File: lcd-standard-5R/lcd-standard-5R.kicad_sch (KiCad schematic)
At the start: 12 parts, among them U1 siplex-som-s16

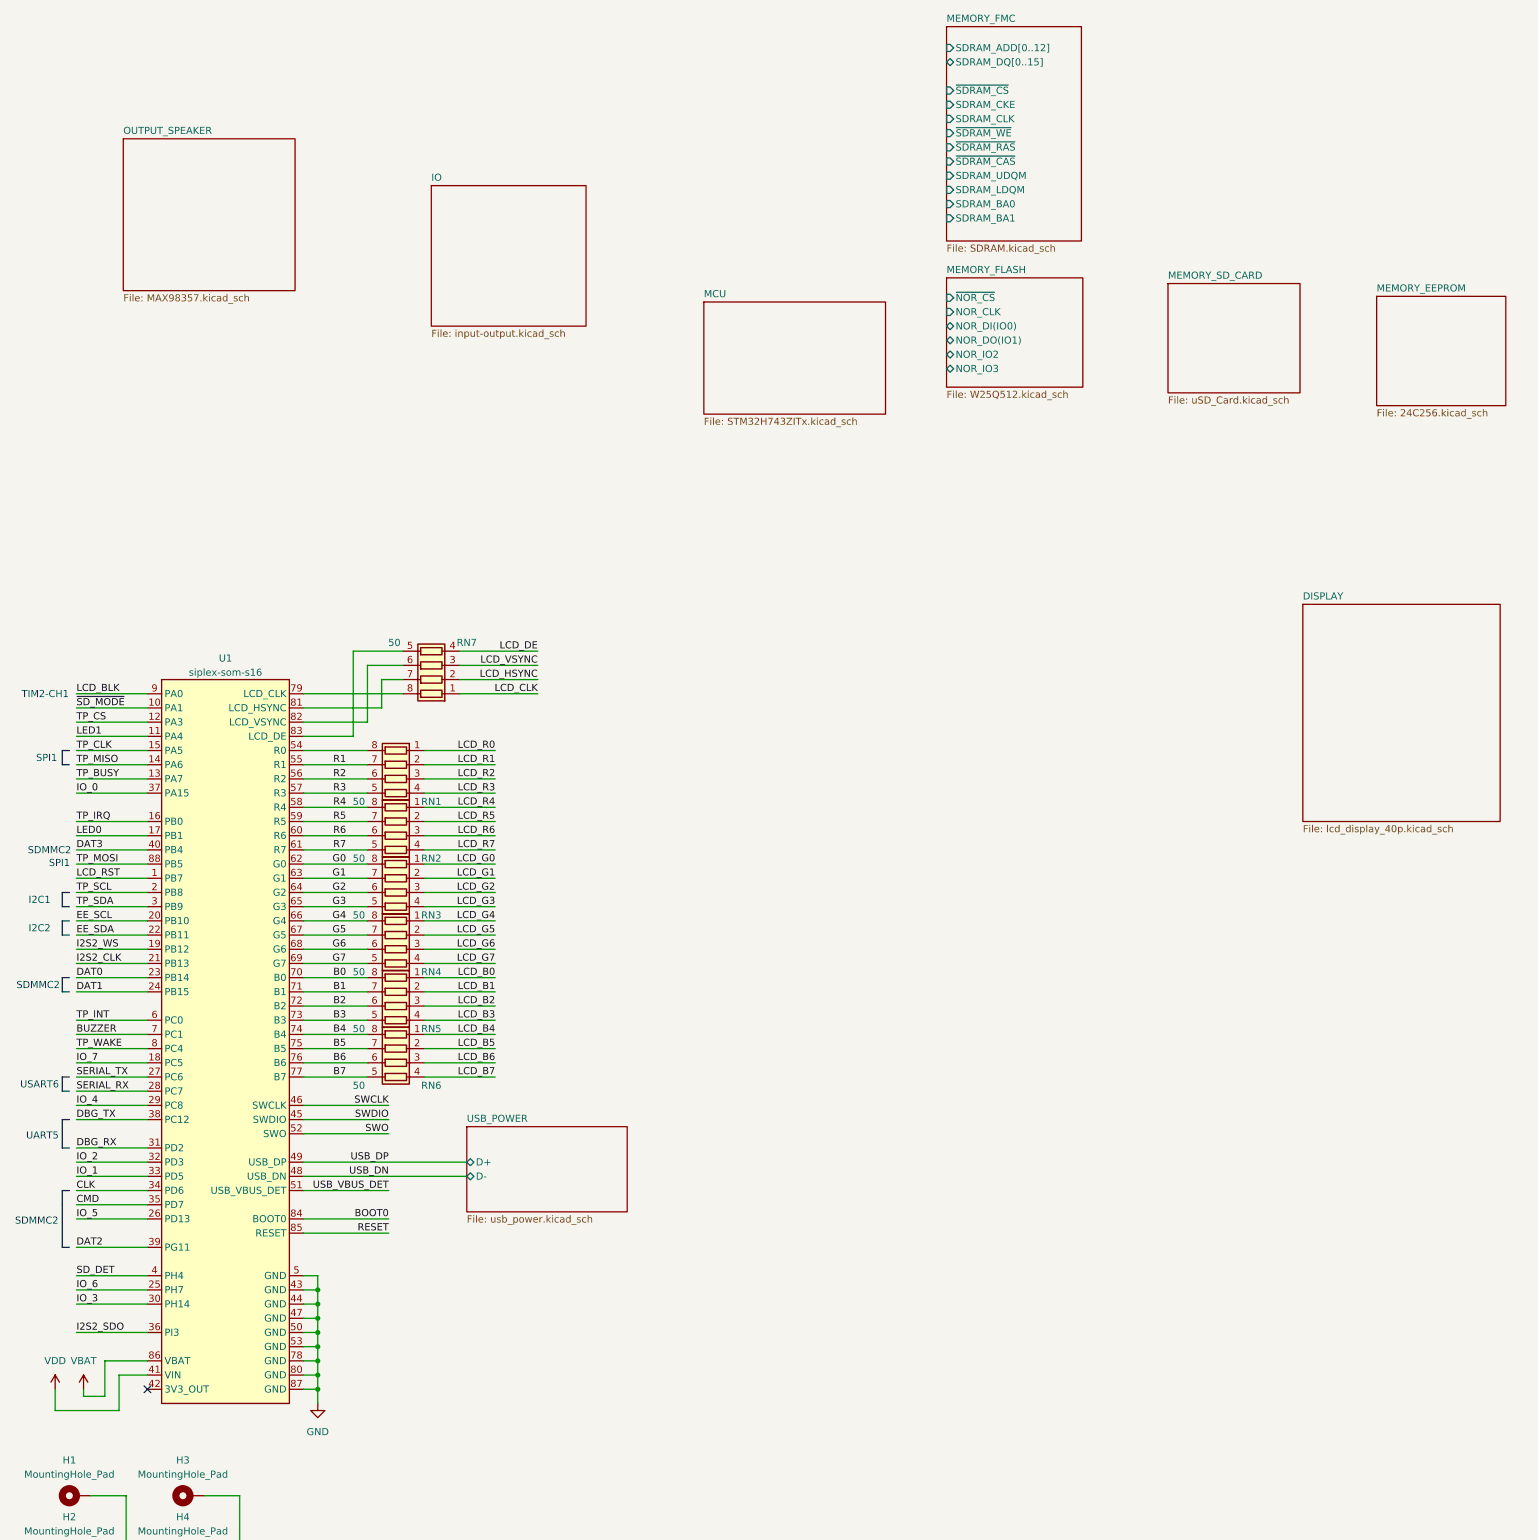
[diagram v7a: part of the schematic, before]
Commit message: Change MCU to STM32H743
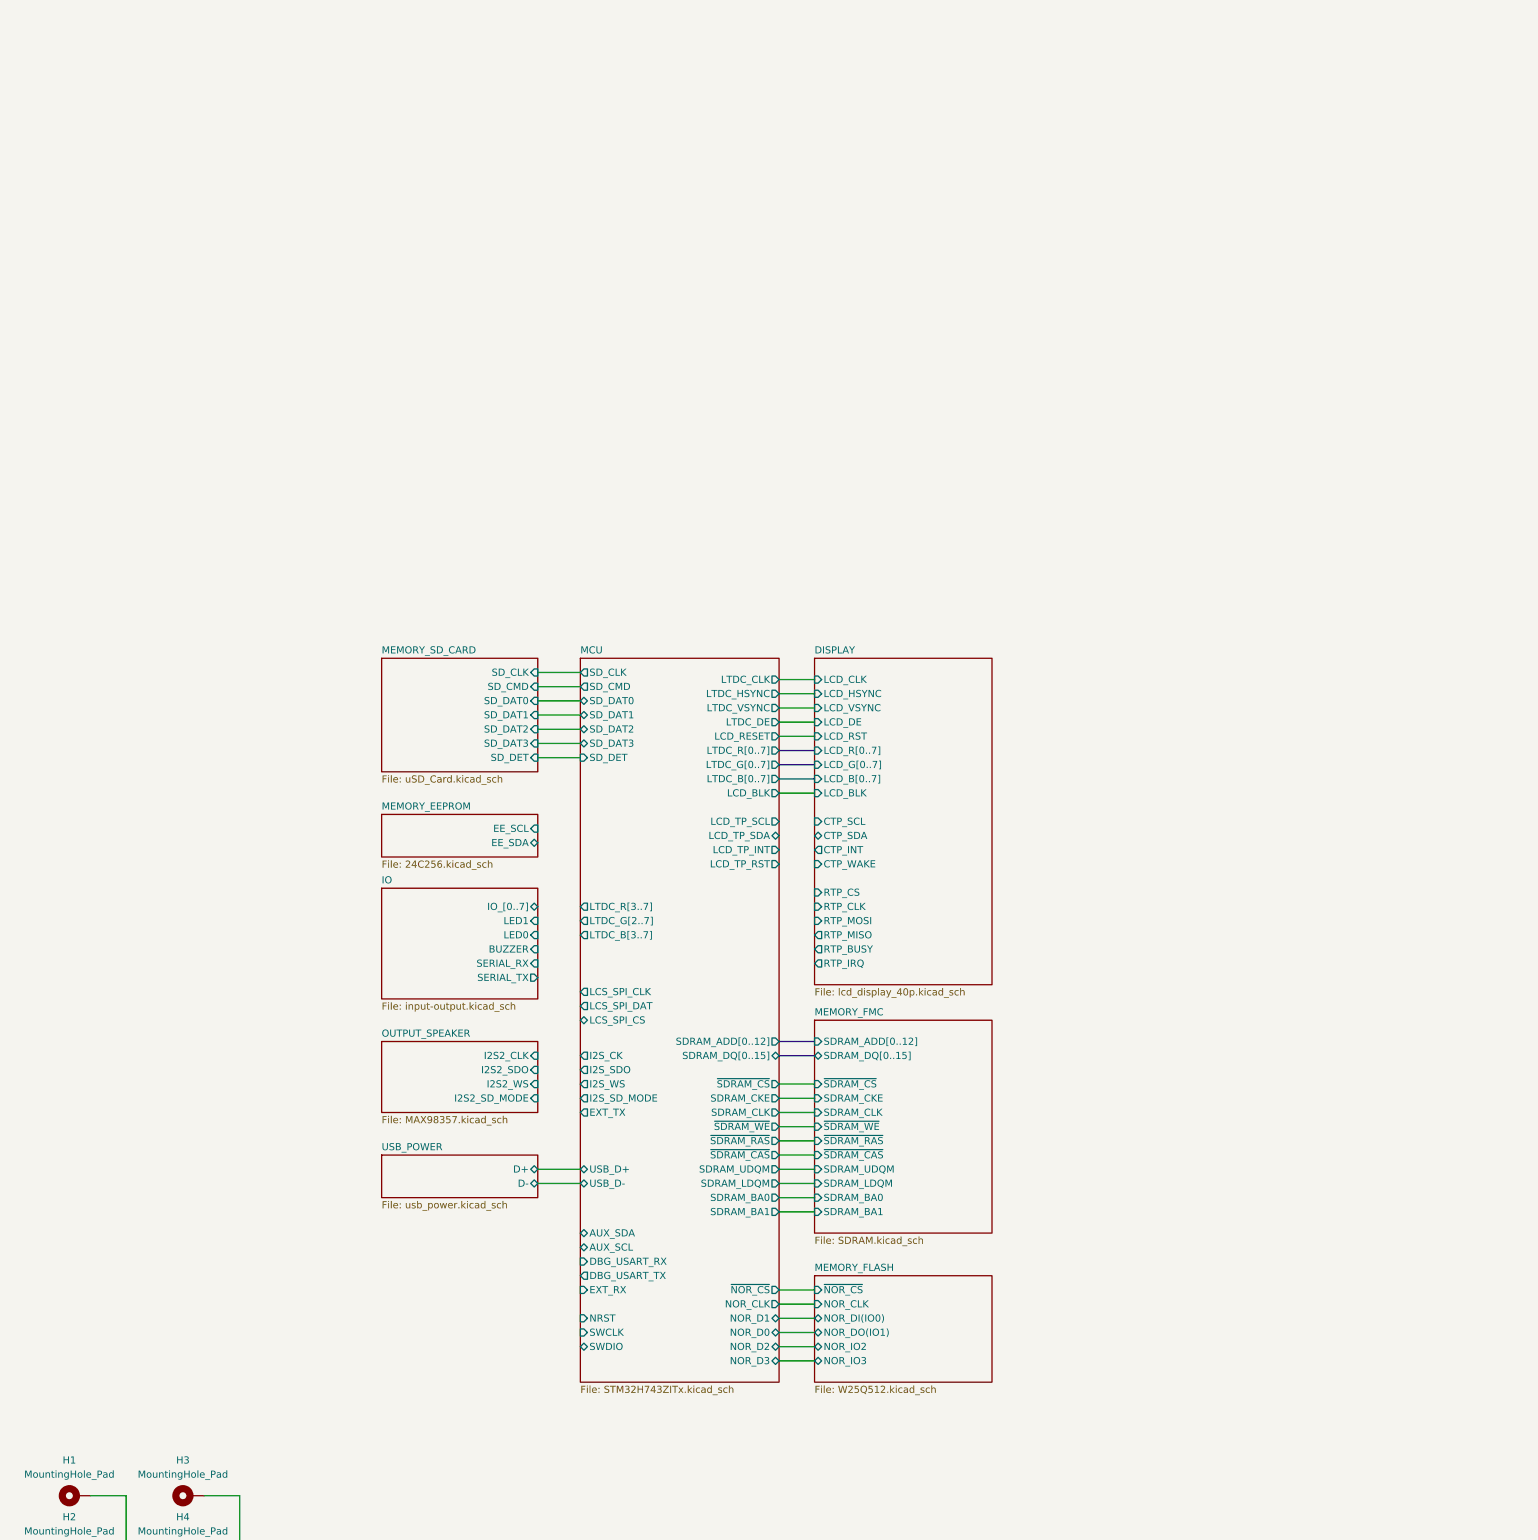
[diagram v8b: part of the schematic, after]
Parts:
- removed RN1, RN2, RN3, RN4, RN5, RN6, RN7: 50, Resistor_SMD:R_Array_Convex_4x0402, symbol Device:R_Pack04
- removed U1: siplex-som-s16, siplex:siplex-som-s16, symbol siplex-som:siplex-som-s16
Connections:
- no-connect marks 1 -> 0
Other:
- sheet DISPLAY ports: added CTP_INT, CTP_SCL, CTP_SDA, CTP_WAKE, LCD_BLK, LCD_B[0..7], LCD_CLK, LCD_DE, LCD_G[0..7], LCD_HSYNC, LCD_RST, LCD_R[0..7], LCD_VSYNC, RTP_BUSY, RTP_CLK, RTP_CS, RTP_IRQ, RTP_MISO, RTP_MOSI; removed none
- sheet IO ports: added BUZZER, IO_[0..7], LED0, LED1, SERIAL_RX, SERIAL_TX; removed none
- sheet MCU ports: added AUX_SCL, AUX_SDA, DBG_USART_RX, DBG_USART_TX, EXT_RX, EXT_TX, I2S_CK, I2S_SDO, I2S_SD_MODE, I2S_WS, LCD_BLK, LCD_RESET, LCD_TP_INT, LCD_TP_RST, LCD_TP_SCL, LCD_TP_SDA, LCS_SPI_CLK, LCS_SPI_CS, LCS_SPI_DAT, LTDC_B[0..7], LTDC_B[3..7], LTDC_CLK, LTDC_DE, LTDC_G[0..7], LTDC_G[2..7], LTDC_HSYNC, LTDC_R[0..7], LTDC_R[3..7], LTDC_VSYNC, NOR_CLK, NOR_D0, NOR_D1, NOR_D2, NOR_D3, NRST, SDRAM_ADD[0..12], SDRAM_BA0, SDRAM_BA1, SDRAM_CKE, SDRAM_CLK, SDRAM_DQ[0..15], SDRAM_LDQM, SDRAM_UDQM, SD_CLK, SD_CMD, SD_DAT0, SD_DAT1, SD_DAT2, SD_DAT3, SD_DET, SWCLK, SWDIO, USB_D+, USB_D-, ~{NOR_CS}, ~{SDRAM_CAS}, ~{SDRAM_CS}, ~{SDRAM_RAS}, ~{SDRAM_WE}; removed none
- sheet MEMORY_EEPROM ports: added EE_SCL, EE_SDA; removed none
- sheet MEMORY_SD_CARD ports: added SD_CLK, SD_CMD, SD_DAT0, SD_DAT1, SD_DAT2, SD_DAT3, SD_DET; removed none
- sheet OUTPUT_SPEAKER ports: added I2S2_CLK, I2S2_SDO, I2S2_SD_MODE, I2S2_WS; removed none
- note removed: "I2C1"
- note removed: "I2C2"
- note removed: "SDMMC2"
- note removed: "SPI1"
- note removed: "TIM2-CH1"
- note removed: "UART5"
- note removed: "USART6"
